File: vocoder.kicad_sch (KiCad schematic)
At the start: 49 parts, among them J1 Micro_SD_Card_Det1, J2 Conn_01x02_Socket, J4 USB_C_Receptacle_USB2.0_16P, J5 Conn_02x03_Top_Bottom, Q3 AO3401A, SW1 SW_Push, SW2 SW_Push, SW3 SW_Push, SW4 RotaryEncoder_Switch, U1 MCP73831-2-MC, U2 AP2112K-3.3, U3 MAX98357A, U4 MAX40200AUK, U7 ESP32-S3-WROOM-1

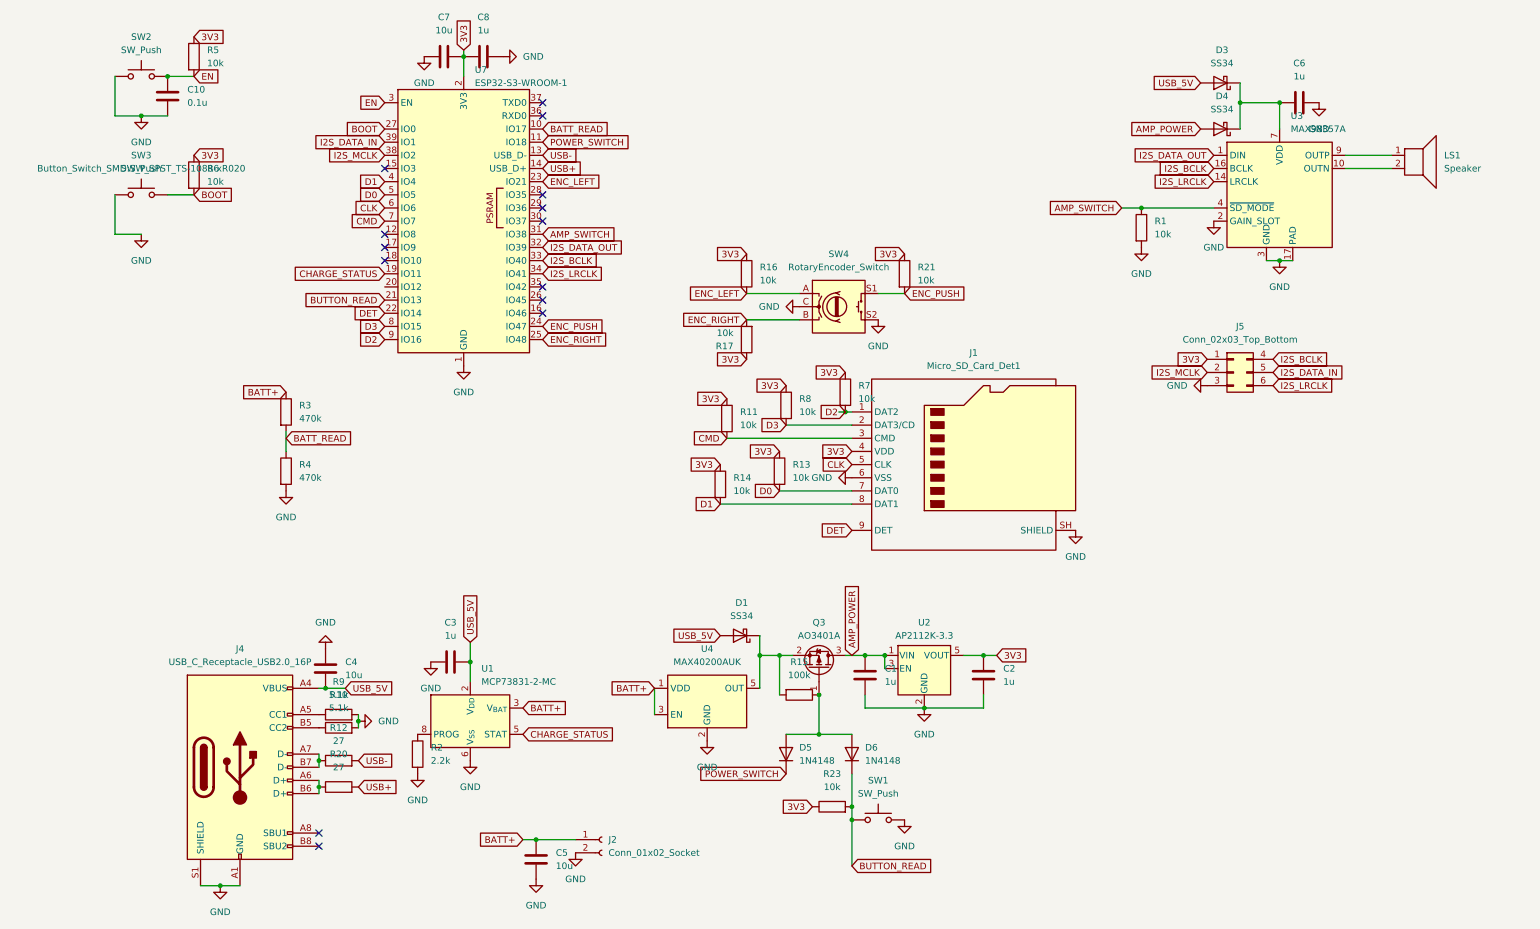
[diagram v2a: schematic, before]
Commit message: reduced board size, removed BMS, will be powered externally only, fixed I2S wiring
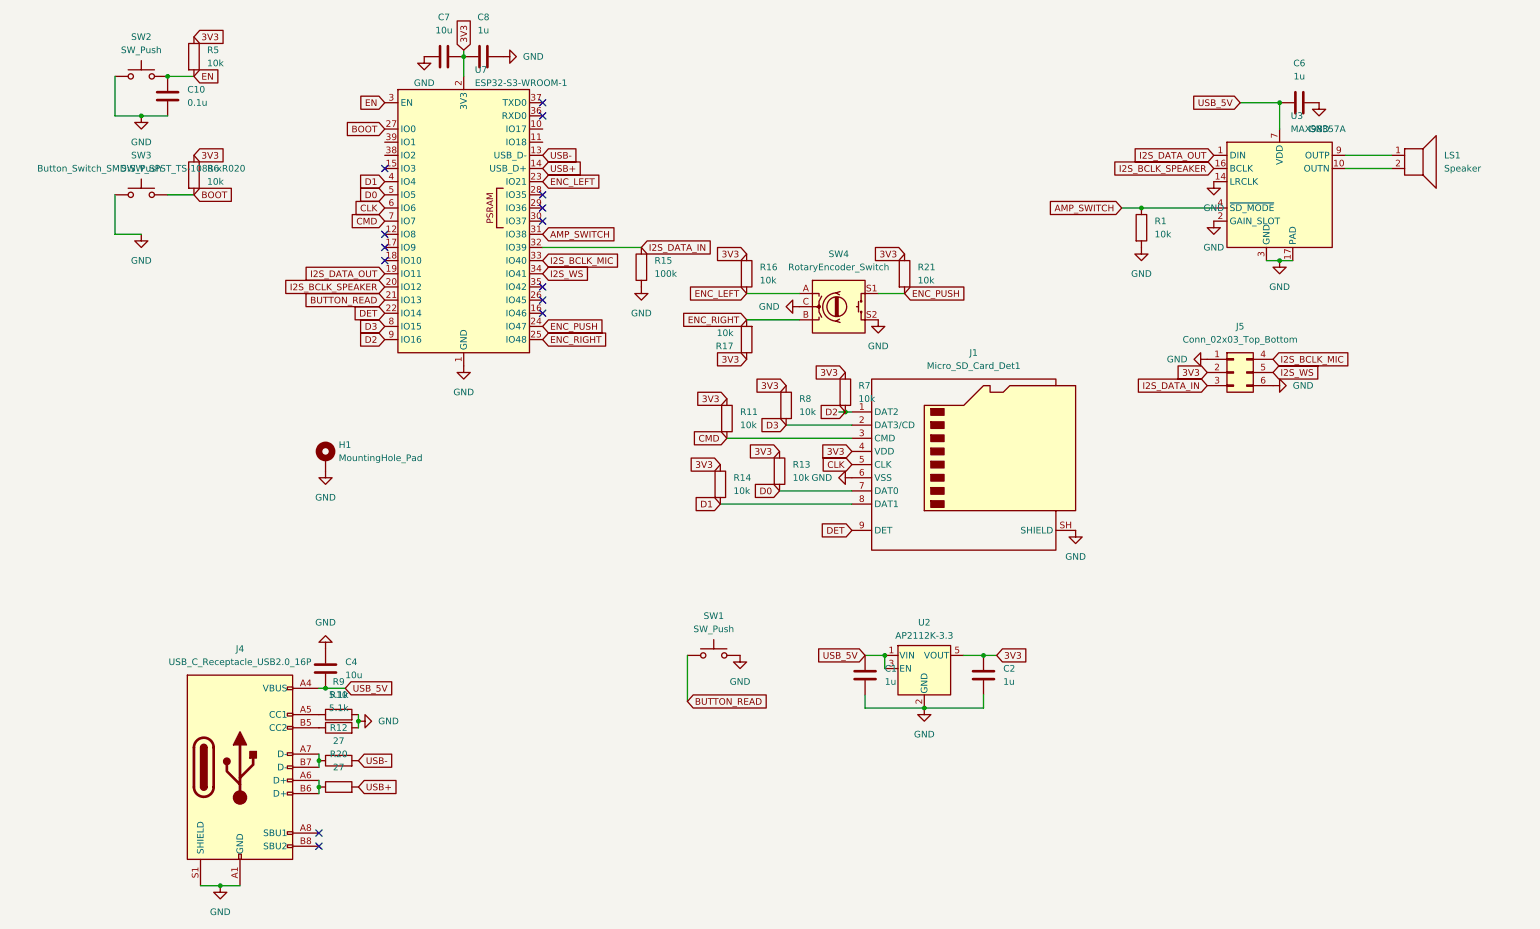
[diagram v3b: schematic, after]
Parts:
- removed C3: 1u, Capacitor_SMD:C_0603_1608Metric, symbol Device:C
- removed C5: 10u, Capacitor_SMD:C_0805_2012Metric, symbol Device:C
- removed D1, D3, D4: SS34, Diode_SMD:D_SOD-123, symbol Diode:SS34
- removed D5, D6: 1N4148, Diode_SMD:D_SOD-323, symbol Diode:1N4148
- removed J2: Conn_01x02_Socket, Connector_PinHeader_2.54mm:PinHeader_1x02_P2.54mm_Vertical, symbol Connector:Conn_01x02_Socket
- removed Q3: AO3401A, Package_TO_SOT_SMD:SOT-23, symbol Transistor_FET:AO3401A
- removed R2: 2.2k, Resistor_SMD:R_0603_1608Metric_Pad0.98x0.95mm_HandSolder, symbol Device:R
- removed R23: 10k, Resistor_SMD:R_0603_1608Metric_Pad0.98x0.95mm_HandSolder, symbol Device:R
- removed R3, R4: 470k, Resistor_SMD:R_0603_1608Metric_Pad0.98x0.95mm_HandSolder, symbol Device:R
- removed U1: MCP73831-2-MC, Package_DFN_QFN:DFN-8-1EP_3x2mm_P0.5mm_EP1.7x1.4mm, symbol Battery_Management:MCP73831-2-MC
- removed U4: MAX40200AUK, Package_TO_SOT_SMD:SOT-23-5, symbol Analog_Switch:MAX40200AUK
- added H1: MountingHole_Pad, MountingHole:MountingHole_3.2mm_M3_DIN965_Pad, symbol Mechanical:MountingHole_Pad
- J5: footprint Connector_PinHeader_2.54mm:PinHeader_2x03_P2.54mm_Vertical -> Connector_PinHeader_2.54mm:PinHeader_1x06_P2.54mm_Vertical
- LS1: footprint TerminalBlock_Phoenix:TerminalBlock_Phoenix_MKDS-1,5-2-5.08_1x02_P5.08mm_Horizontal -> Connector_PinHeader_2.54mm:PinHeader_1x02_P2.54mm_Vertical
- SW1: footprint Button_Switch_SMD:Panasonic_EVQPUJ_EVQPUA -> Button_Switch_THT:SW_Tactile_SPST_Angled_PTS645Vx58-2LFS
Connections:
- net AMP_POWER is gone; now on net USB_5V: C1.1, U2.1 (VIN), U2.3 (EN)
- net CHARGE_STATUS is gone; now on net I2S_DATA_OUT: U7.19 (IO11)
- net 3V3: now also J5.2 (Pin_2); no longer J5.1 (Pin_1)
- net GND: now also J5.1 (Pin_1), J5.6 (Pin_6), R15.1, U3.14 (LRCLK), H1.1; no longer J5.3 (Pin_3)
- net I2S_DATA_IN: now also J5.3 (Pin_3), R15.2, U7.32 (IO39); no longer J5.5 (Pin_5), U7.39 (IO1)
- net I2S_DATA_OUT: no longer U7.32 (IO39)
- net USB_5V: now also C6.1, U3.7 (VDD), U3.8 (VDD)
- net I2S_BCLK_SPEAKER: now reaches U7.20 (IO12)
- net I2S_BCLK_SPEAKER: now also U3.16 (BCLK)
- net BATT_READ: no longer names the net of U7.10 (IO17)
- net I2S_BCLK renamed I2S_BCLK_MIC
- net I2S_BCLK_MIC: no longer U3.16 (BCLK)
- removed net I2S_LRCLK: J5.6 (Pin_6), U3.14 (LRCLK), U7.34 (IO41)
- net I2S_MCLK: no longer names the net of U7.38 (IO2)
- net I2S_MCLK: no longer J5.2 (Pin_2)
- net POWER_SWITCH: no longer names the net of U7.11 (IO18)
- new net I2S_WS: J5.5 (Pin_5), U7.34 (IO41)
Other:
- moved on the sheet: SW1
